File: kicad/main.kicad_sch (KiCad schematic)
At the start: 16 parts, among them J1 Conn_battery, J2 AudioJack3, SW1 SW_Push, U1 TPS73101DBV, U2 ESP32-WROOM-32

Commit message: feat: schematic, pcb layout, code, enclosure
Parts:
- removed U2: ESP32-WROOM-32, RF_Module:ESP32-C3-WROOM-02U, symbol RF_Module:ESP32-WROOM-32
- added J3: USB_PWR, Connector_Wire:SolderWire-1.5sqmm_1x02_P6mm_D1.7mm_OD3mm, symbol Connector:Conn_01x02_Socket
- added U2: ESP32_DevKit_V1, !my-kicad-library:esp32_devkit_v1_doit, symbol !my-kicad-library:ESP32_DevKit_V1
- BZ1: footprint (none) -> !my-kicad-library:Buzzer-GT-0905A
- D1: footprint Diode_THT:D_DO-35_SOD27_P7.62mm_Horizontal -> Diode_SMD:D_MELF
- J1: footprint (none) -> Connector_Wire:SolderWire-1.5sqmm_1x02_P6mm_D1.7mm_OD3mm
- J2: footprint (none) -> Connector_Audio:Jack_3.5mm_CUI_SJ1-3535NG_Horizontal
- SW1: footprint (none) -> Button_Switch_THT:SW_PUSH_6mm
- gave numbers to parts that had none: 2
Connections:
- net RAW_PWR is gone; now on an unnamed net: J1.2 (Pin_2), U1.1 (IN)
- net BATTERY_SENSE: now also U2.2 (SENSOR_VP)
- net BTN_SENSE: now also U2.25 (IO19)
- net DAH: now also U2.7 (IO33)
- net DIT: now also U2.6 (IO32)
- net GND: now also J1.1 (Pin_1), J3.1 (Pin_1), U2.14 (GND), U2.17 (GND)
- net PWR_LATCH: now also U2.24 (IO18)
- net VDD: now also R1.1, U2.16 (3V3)
- net at SW1.1: no longer R3.1
- net BUZZER: no longer names the net of BZ1.1 (+)
- net BUZZER: now also U2.22 (IO17)
- new net: R3.1, SW1.2
- new net VIN: J3.2 (Pin_2), U2.15 (VIN)
- no-connect marks 23 -> 20
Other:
- note removed: "internal pullup"
- moved on the sheet: BZ1, D1, J1, J2, R1, R2, R3, R4, R9, SW1

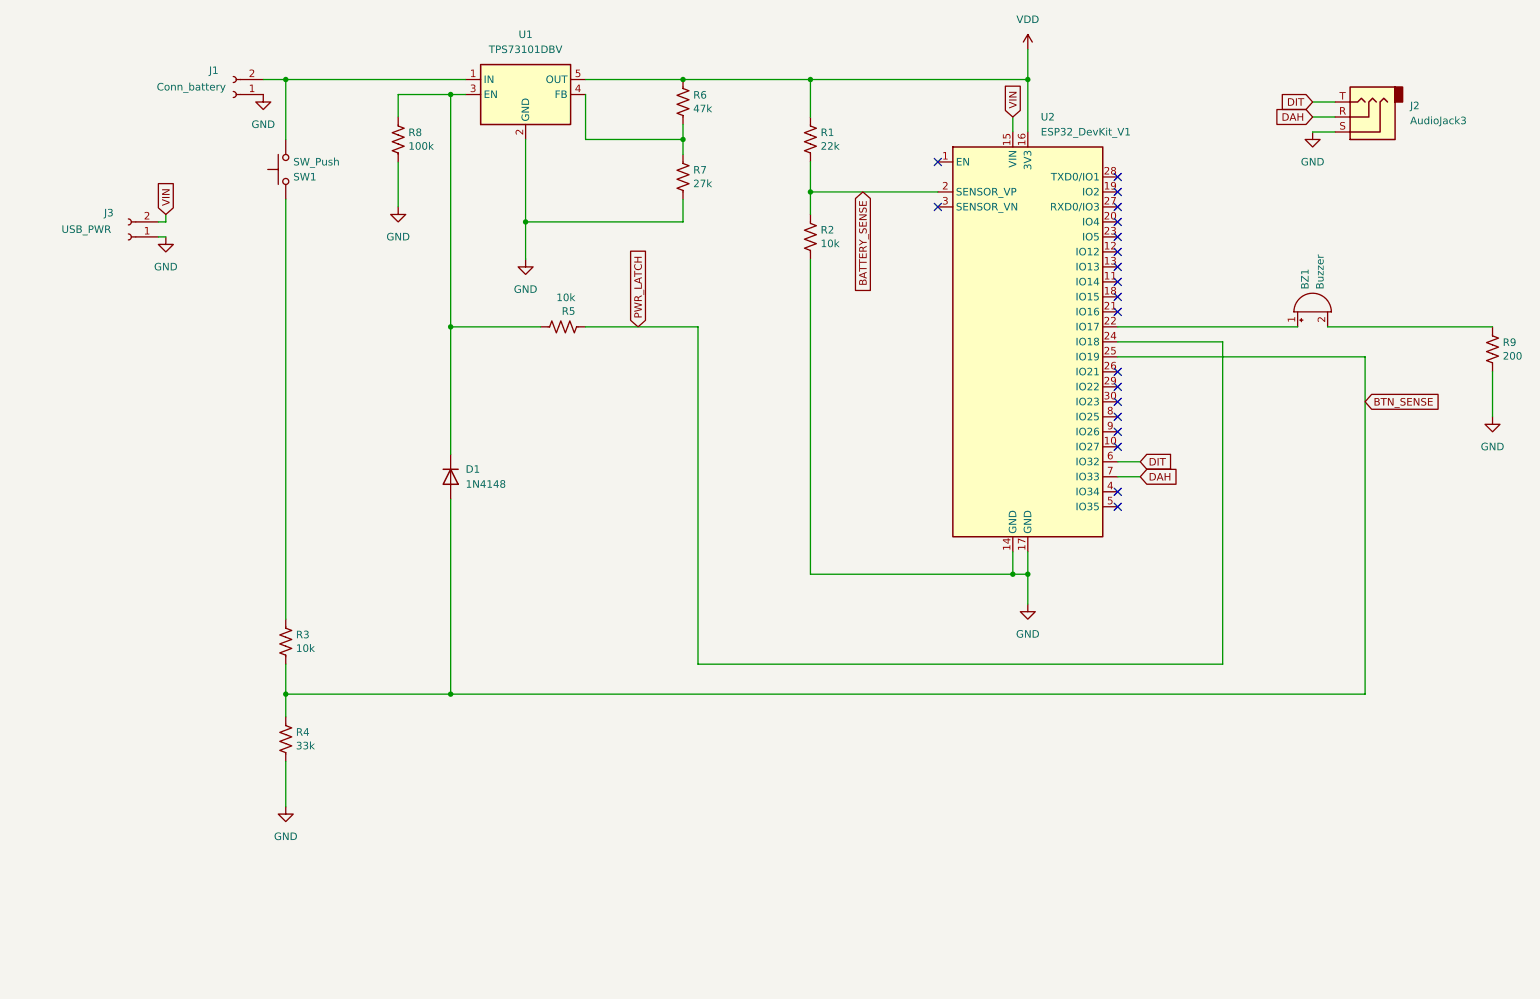
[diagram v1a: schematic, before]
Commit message: feat: update schematic with protection RC
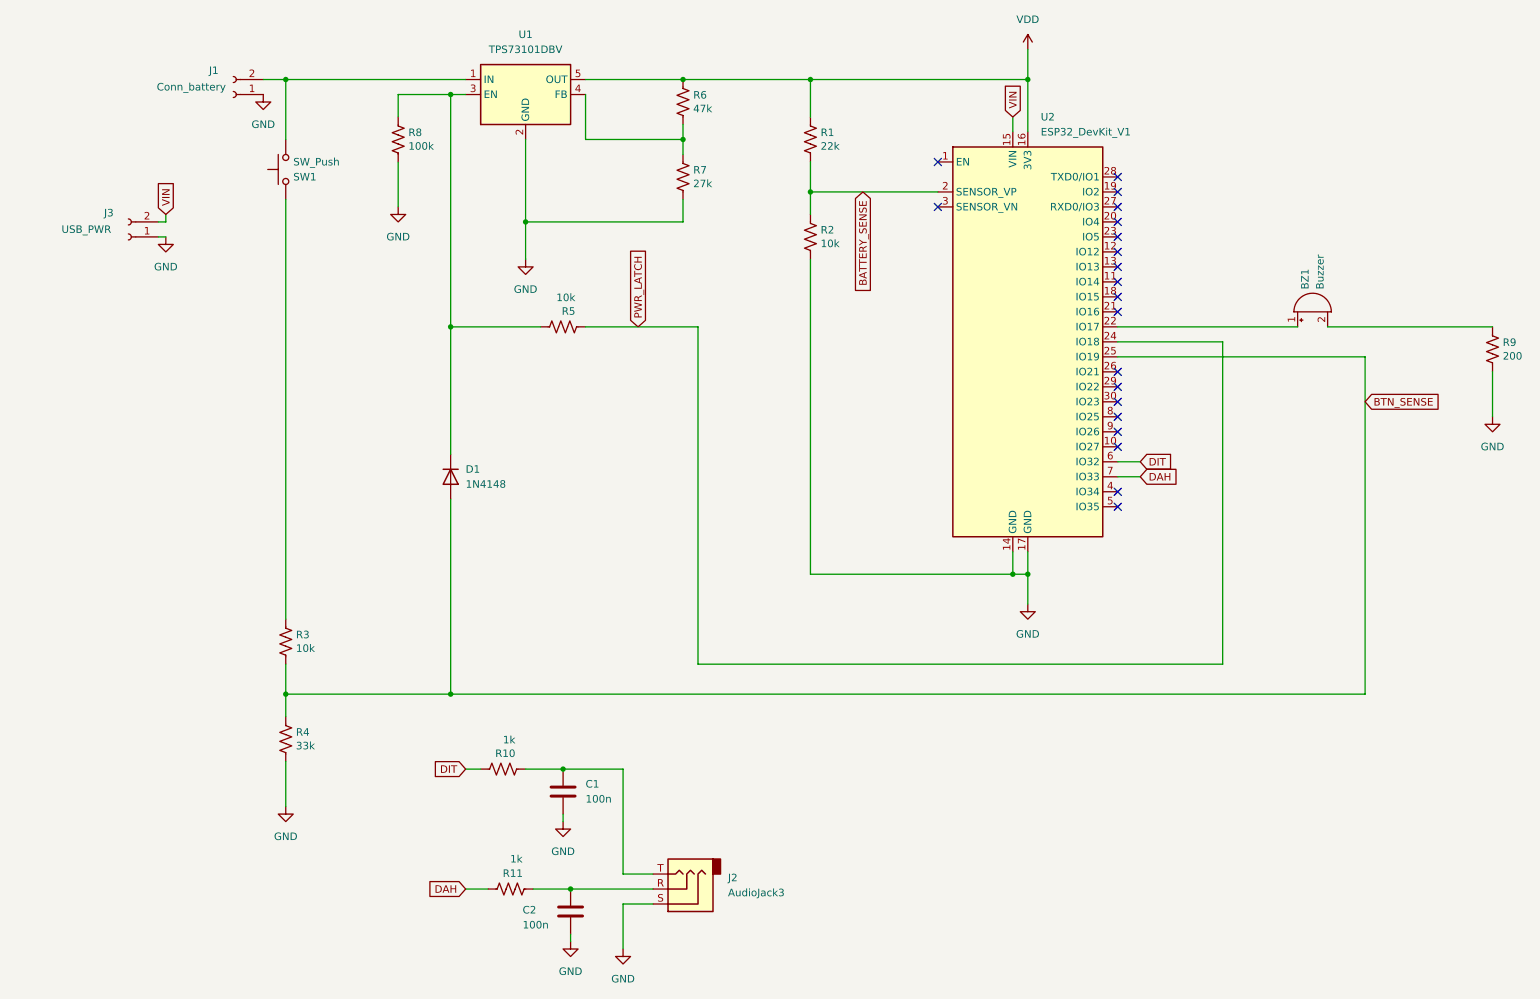
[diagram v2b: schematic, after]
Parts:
- added C1, C2: 100n, Capacitor_SMD:C_1206_3216Metric, symbol Device:C
- added R10, R11: 1k, Resistor_SMD:R_0805_2012Metric, symbol Device:R_US
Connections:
- net DAH: now also R11.1; no longer J2.R
- net DIT: now also R10.1; no longer J2.T
- net GND: now also C1.2, C2.2
- new net: C1.1, J2.T, R10.2
- new net: C2.1, J2.R, R11.2
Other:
- moved on the sheet: J2
